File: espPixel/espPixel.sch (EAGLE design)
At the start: 78 parts, among them IC1 74LVC1T45GW,125, IC2 74LVC1T45GW,125, IC3 MP2315GJ-Z, IC4 CP2104, J1 TBLH10-350-04BK, J2 TBLH10-350-03BK, J3 TBLH10-350-02BK, Q1 SIR414DP-T1-GE3, Q2 SIR414DP-T1-GE3, Q5 mmbt2222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

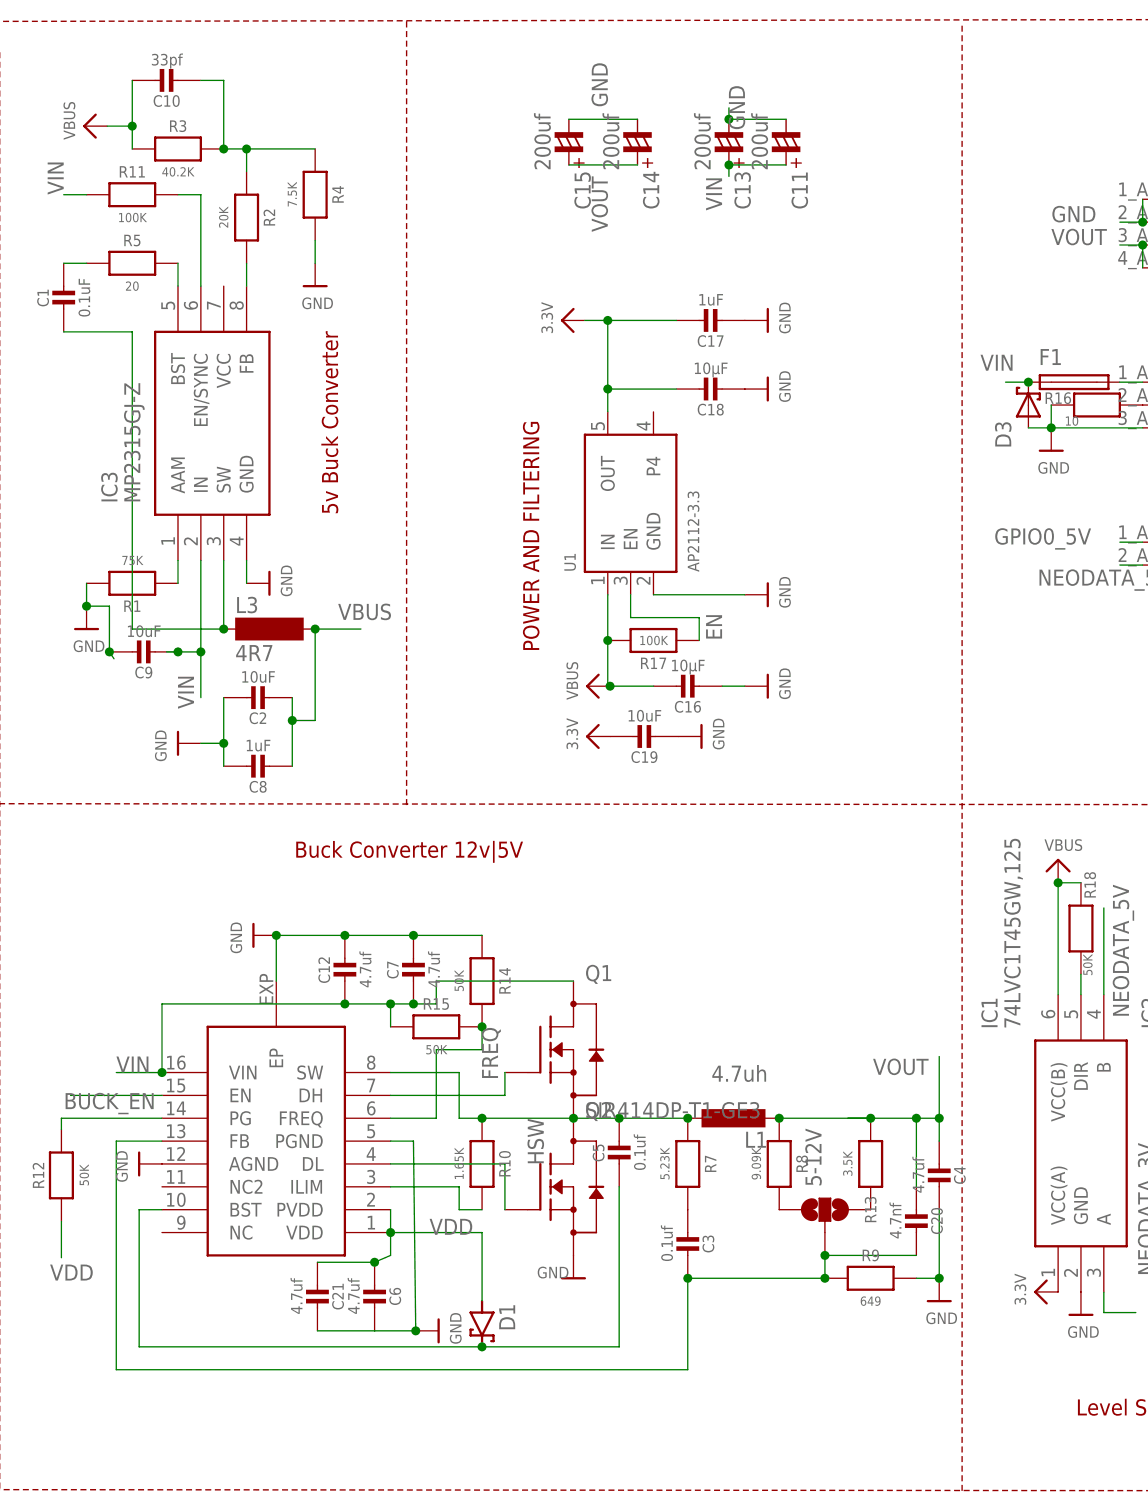
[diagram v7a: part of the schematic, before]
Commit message: More filter caps
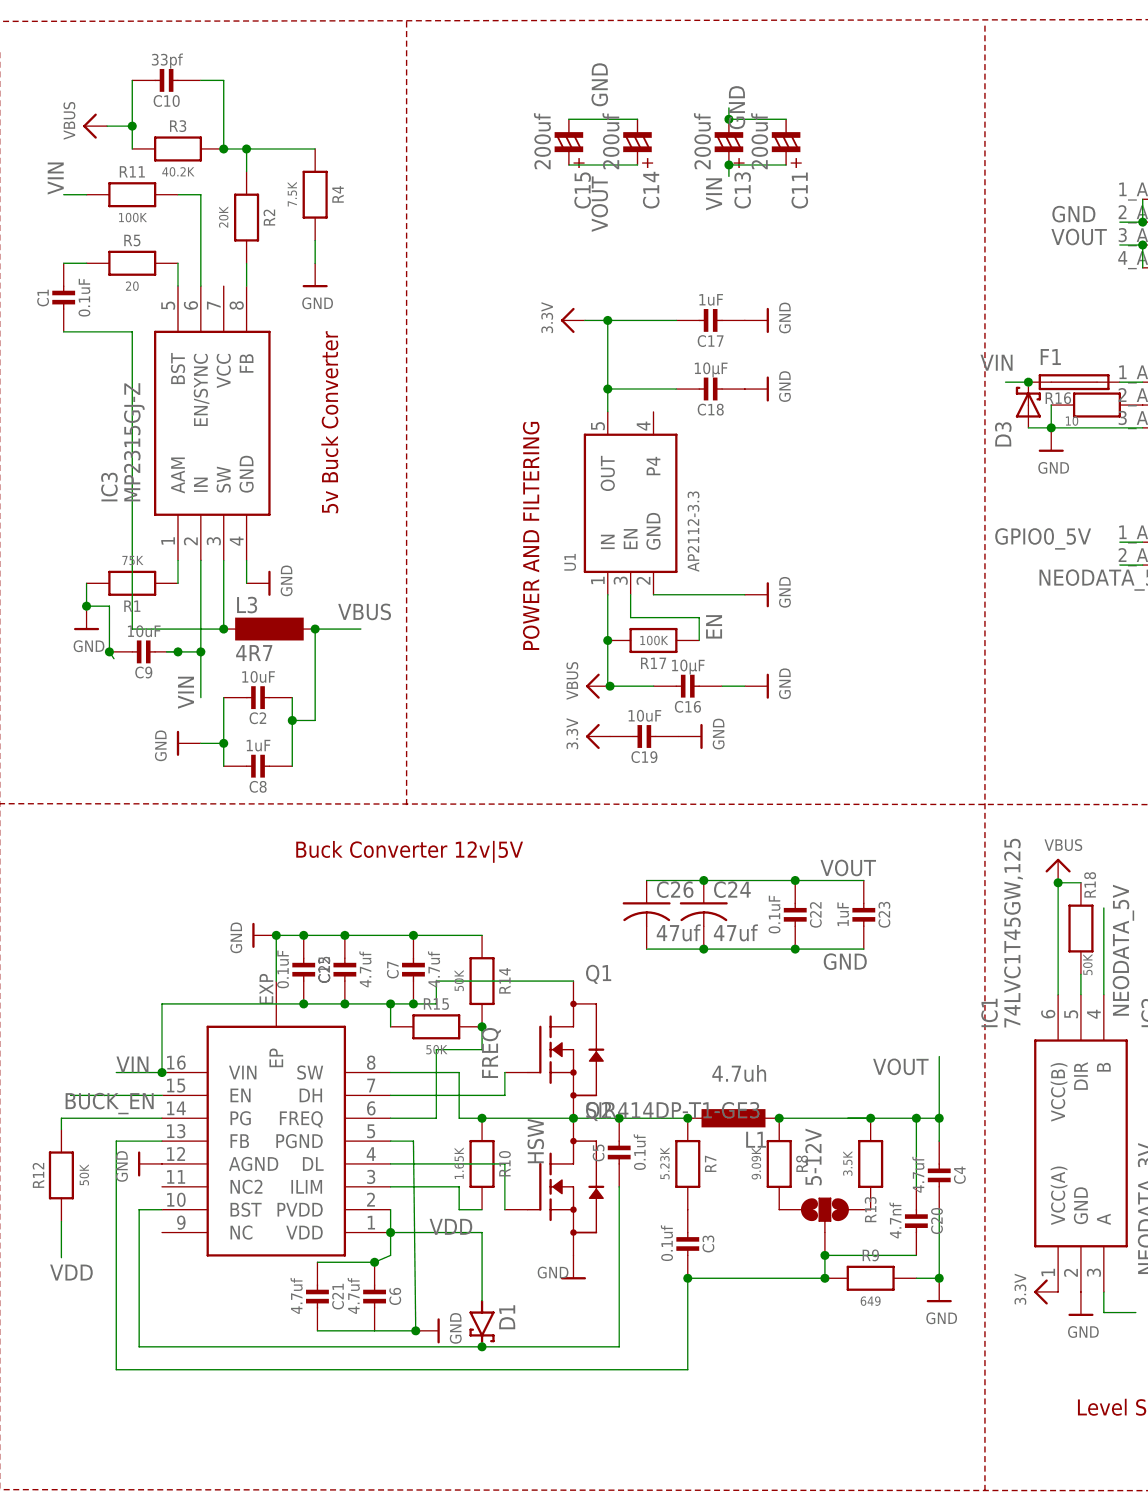
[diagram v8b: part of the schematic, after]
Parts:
- added C22, C25: 0.1uF, microbuilder:CAP_CERAMIC0603_NO
- added C23: 1uF, microbuilder:CAP_CERAMIC0603_NO
- added C24, C26: 47uf, adafruit:C-USC3225
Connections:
- net GND: now also C22.1, C23.1, C24.2, C25.2, C26.2
- net VIN: now also C25.1
- net VOUT: now also C22.2, C23.2, C24.1, C26.1
